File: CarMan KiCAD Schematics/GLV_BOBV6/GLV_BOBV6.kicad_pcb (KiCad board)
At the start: 2 copper layers, 79.5 x 60.3 mm, 26 parts, among them J1 LSP Conn_01x02, J2 Extra 24V Conn_01x02, J3 CAN ISO Conn_01x02, J4 Logic Conn_02x02_Odd_Even, J5 TSI Conn_02x02_Odd_Even, J6 Breakers J6, U1 INA226AIDGSR

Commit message: Logic, TSI & GLV revisions
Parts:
- removed D1: LED, CarMan General Footprints:VAOL-S8GT4
- removed J1 LSP: Conn_01x02, CarMan General Footprints:Molex_MiniFit-JR-5556-02A_2x01x4.20mm_Straight
- removed J6 Breakers: J6, CarMan General Footprints:Molex_MiniFit-JR-5556-06A_2x03x4.20mm_Straight
- removed R4: 2K, Resistor_SMD:R_0805_2012Metric_Pad1.15x1.40mm_HandSolder
- removed R5: 3.9K, Resistor_SMD:R_0805_2012Metric_Pad1.15x1.40mm_HandSolder
- removed R7: 10K, Resistor_SMD:R_0805_2012Metric_Pad1.15x1.40mm_HandSolder
- added J1: Conn_01x02, CarMan General Footprints:Molex_Mega-Fit_76829-0102_2x01_P5.70mm_Vertical, F.Cu at (132.1, 21.6)
- added J6: J6, CarMan General Footprints:Molex_Mega-Fit_76829-0106_2x03_P5.70mm_Vertical, F.Cu at (139.7, 62.9)
- J2: renamed from J2 Extra 24V
- J3: renamed from J3 CAN ISO
- J4: renamed from J4 Logic
- J5: renamed from J5 TSI
- moved J5 2.86 mm to (132.8, 39.6), turned to 270 degrees
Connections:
- C1 pad 1: /3.3V_NOT_ISO -> /5V_NON_ISO
- C3 pad 2: /5V_NOT_ISO -> /5V_NON_ISO
- CR1 pad 1: /5V_NOT_ISO -> /5V_NON_ISO
- R2 pad 1: /3.3V_NOT_ISO -> /5V_NON_ISO
- R3 pad 1: /3.3V_NOT_ISO -> /5V_NON_ISO
- R8 pad 2: /5V_NOT_ISO -> /5V_NON_ISO
- U1 pad 6: /3.3V_NOT_ISO -> /5V_NON_ISO
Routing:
- net /5V_NON_ISO: track 0.00 -> 62.2 mm, vias 0 -> 2
- net /3.3V_NOT_ISO: track 46.1 -> 0.00 mm, vias 2 -> 0
- net /5V_NOT_ISO: track 26.8 -> 0.00 mm
- net /GLV_RTN: track 74.3 -> 58.8 mm
- net /BREAKER_OUT_SL: track 15.4 -> 29.4 mm
- net /24V: track 167.5 -> 158.2 mm
- net /24V_NOT_BREAKERED: track 56.4 -> 60.6 mm
- net Net-(D1-Pad2): track 3.03 -> 0.00 mm
- net /BREAKER_OUT_COOL: track 15.4 -> 16.1 mm
- net /SDA_NOT_ISO: vias 3 -> 2
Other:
- board text added: "GLV BOB v. 7.0 Troy Coleman and Zachary Martin 4/26/21"
- board text removed: "GLV BOB V6.0 Troy Coleman and Zachary Martin 2/9/21"

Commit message: Aesthetics
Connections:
- CR1 pad 4: Net-(CR1-Pad4) -> (no net)
- CR1 pad 5: Net-(CR1-Pad5) -> (no net)
- R2 pad 2: /SCL_NOT_ISO -> /SDA_NOT_ISO
- R3 pad 2: /SDA_NOT_ISO -> /SCL_NOT_ISO
- U1 pad 3: Net-(U1-Pad3) -> (no net)
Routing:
- net /SDA_NOT_ISO: track 37.0 -> 42.1 mm
- net /24V: track 158.2 -> 160.5 mm
- net /SCL_NOT_ISO: track 39.6 -> 41.0 mm, vias 2 -> 3
- net /24V_NOT_BREAKERED: track 60.6 -> 61.9 mm

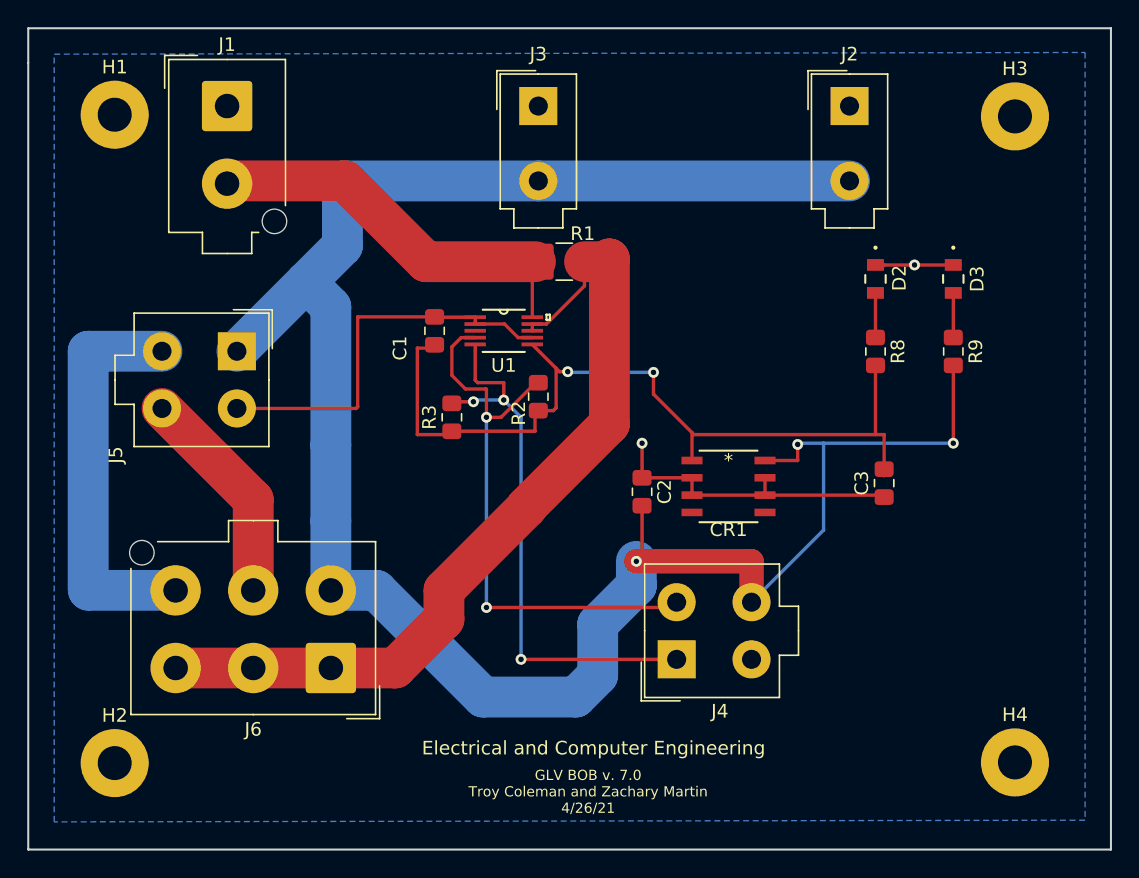
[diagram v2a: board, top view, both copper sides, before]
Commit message: Fixed GLV header names
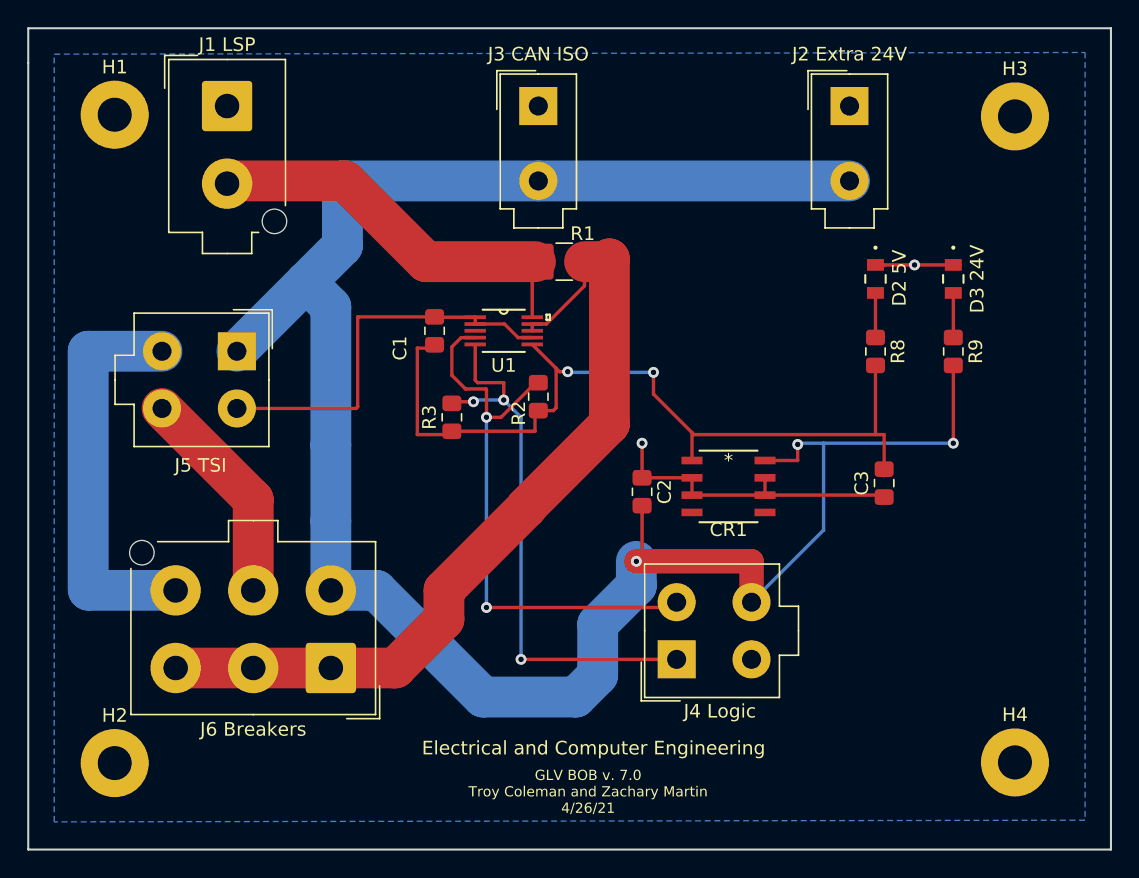
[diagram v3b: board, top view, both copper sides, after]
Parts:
- D2 5V: renamed from D2
- D3 24V: renamed from D3
- J1 LSP: renamed from J1
- J2 Extra 24V: renamed from J2
- J3 CAN ISO: renamed from J3
- J4 Logic: renamed from J4
- J5 TSI: renamed from J5
- J6 Breakers: renamed from J6
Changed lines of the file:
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@@
-(kicad_pcb (version 20171130) (host pcbnew "(5.1.6)-1")
+(kicad_pcb (version 20171130) (host pcbnew "(5.1.2)-1")
   (general
     (thickness 1.6)
@@
   (module "CarMan General Footprints:VAOL-S8GT4" (layer F.Cu)
     (at 179.705 34.29 270)
-    (fp_text reference D2 (at -0.071101 -1.752501 90) (layer F.SilkS)
+    (fp_text reference "D2 5V" (at -0.071101 -1.752501 90) (layer F.SilkS)
       (effects (font (size 1 1) (thickness 0.15)))
     )
@@
   (module "CarMan General Footprints:VAOL-S8GT4" (layer F.Cu)
     (at 185.42 34.29 270)
-    (fp_text reference D3 (at 0 -1.752501 90) (layer F.SilkS)
+    (fp_text reference "D3 24V" (at 0 -1.752501 90) (layer F.SilkS)
       (effects (font (size 1 1) (thickness 0.15)))
     )
@@
     (descr "Molex Mini-Fit JR, PN:5556-02A, dual row, top entry type, through hole")
     (tags "connector molex mini-fit 5556")
-    (fp_text reference J2 (at 0 -3.81) (layer F.SilkS)
+    (fp_text reference "J2 Extra 24V" (at 0 -3.81) (layer F.SilkS)
       (effects (font (size 1 1) (thickness 0.15)))
     )
@@
     (descr "Molex Mini-Fit JR, PN:5556-02A, dual row, top entry type, through hole")
     (tags "connector molex mini-fit 5556")
-    (fp_text reference J3 (at 0 -3.81) (layer F.SilkS)
+    (fp_text reference "J3 CAN ISO" (at 0 -3.81) (layer F.SilkS)
       (effects (font (size 1 1) (thickness 0.15)))
     )
@@
     (descr "Molex Mini-Fit JR, PN:5556-04A, dual row, top entry type, through hole")
     (tags "connector molex mini-fit 5556")
-    (fp_text reference J4 (at -3.81 3.175 180) (layer F.SilkS)
+    (fp_text reference "J4 Logic" (at -3.81 3.175 180) (layer F.SilkS)
       (effects (font (size 1 1) (thickness 0.15)))
     )
@@
     (descr "Molex Mini-Fit JR, PN:5556-04A, dual row, top entry type, through hole")
     (tags "connector molex mini-fit 5556")
-    (fp_text reference J5 (at 7.62 8.89 90) (layer F.SilkS)
+    (fp_text reference "J5 TSI" (at 8.382 2.667 180) (layer F.SilkS)
       (effects (font (size 1 1) (thickness 0.15)))
     )
@@
     (descr "Molex Mega-Fit Power Connectors, 76829-0102 (compatible alternatives: 172065-0202, 172065-0302), 1 Pins per row (http://www.molex.com/pdm_docs/sd/768290102_sd.pdf), generated with kicad-footprint-generator")
     (tags "connector Molex Mega-Fit side entry")
-    (fp_text reference J1 (at 0 -4.51) (layer F.SilkS)
+    (fp_text reference "J1 LSP" (at 0 -4.51) (layer F.SilkS)
       (effects (font (size 1 1) (thickness 0.15)))
     )
@@
     (descr "Molex Mega-Fit Power Connectors, 76829-0106 (compatible alternatives: 172065-0206, 172065-0306), 3 Pins per row (http://www.molex.com/pdm_docs/sd/768290102_sd.pdf), generated with kicad-footprint-generator")
     (tags "connector Molex Mega-Fit side entry")
-    (fp_text reference J6 (at 5.7 -4.51) (layer F.SilkS)
-      (effects (font (size 1 1) (thickness 0.15)))
-    )
+    (fp_text reference "J6 Breakers" (at 5.7 -4.51) (layer F.SilkS)
+      (effects (font (size 1 1) (thickness 0.15)))
+    )

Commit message: Gerber Files
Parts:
- added G***: LOGO, CarMan General Footprints:Laf_College_Logo, F.Cu at (184.6, 60.2)
- added VAL: REF, CarMan General Footprints:lafLogo, F.Cu at (178.0, 70.3)
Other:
- board text added: "GLV BOB v. 7"
- board text added: "GLV BOB v. 7.0 Troy Coleman and Zachary Martin 4/27/21"
- board text added: "Made in USA"
- board text removed: "GLV BOB v. 7.0 Troy Coleman and Zachary Martin 4/26/21"

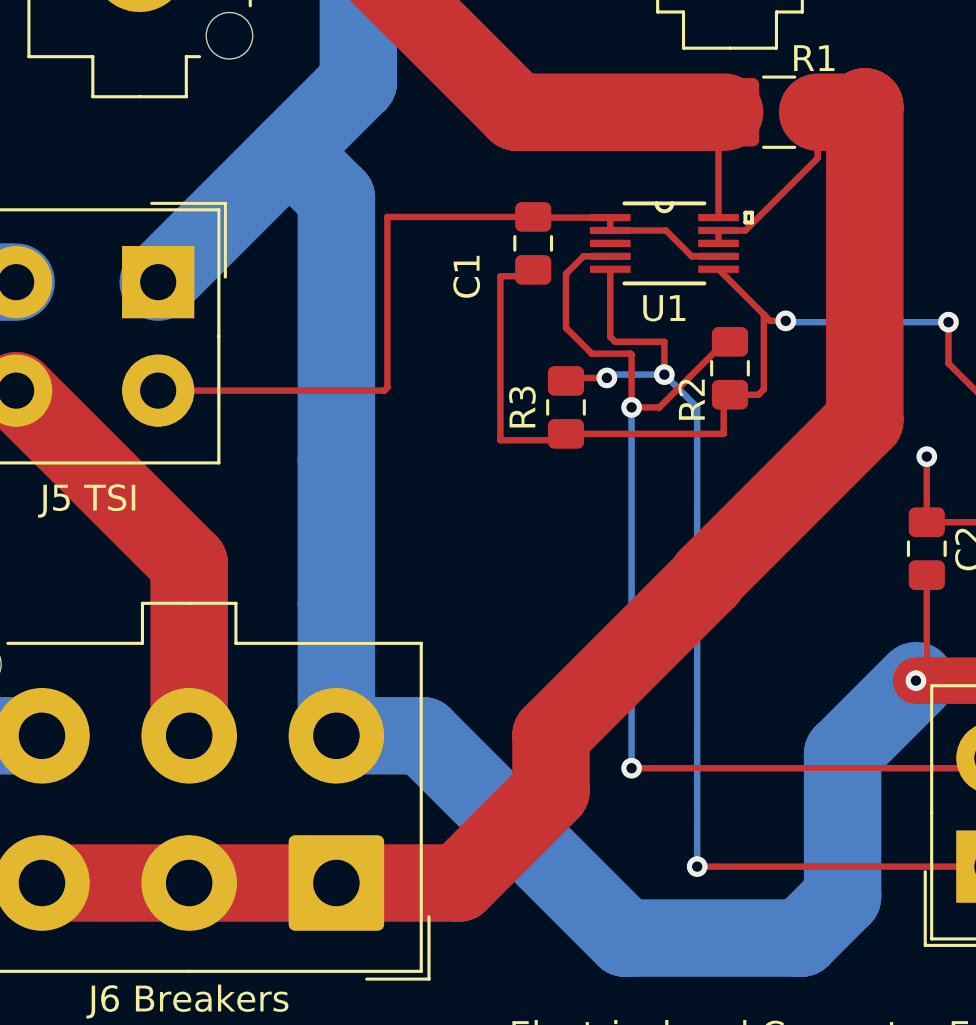
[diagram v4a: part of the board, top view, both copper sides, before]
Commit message: updated GLV bypass cap current sensor
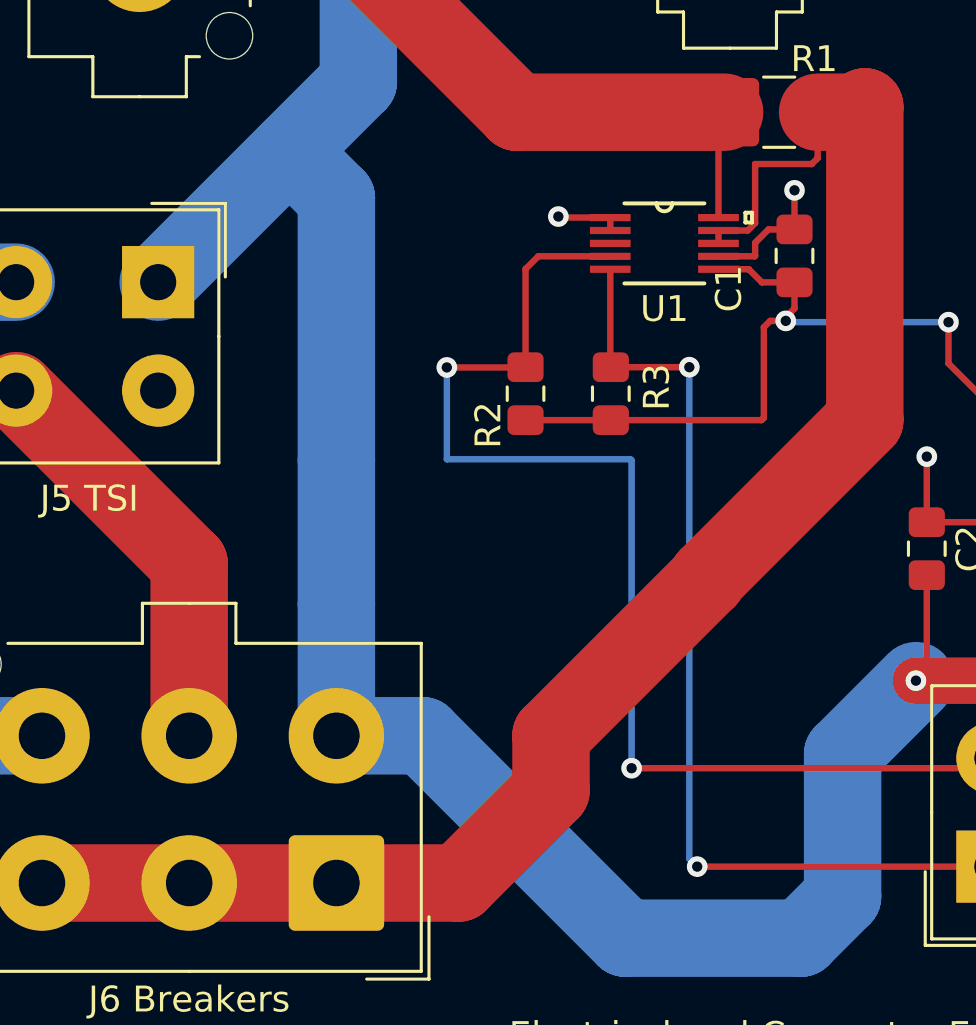
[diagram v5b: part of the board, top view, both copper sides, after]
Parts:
- moved C1 10.1 mm to (157.4, 38.6)
- moved R2 7.98 mm to (147.0, 43.9)
- moved R3 1.82 mm to (150.3, 43.9)
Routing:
- net /GLV_RTN: track 58.8 -> 37.2 mm, vias 2 -> 4
- net /5V_NON_ISO: track 62.2 -> 54.8 mm
- net /SDA_NOT_ISO: track 42.1 -> 47.1 mm
- net /SCL_NOT_ISO: track 41.0 -> 37.7 mm, vias 3 -> 2
- net /24V_NOT_BREAKERED: track 61.9 -> 63.2 mm
